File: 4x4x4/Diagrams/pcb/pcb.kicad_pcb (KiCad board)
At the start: 2 copper layers, 65.3 x 145.8 mm, 77 parts, among them J1 Conn_01x04_Female, J10 Conn_01x04_Female, J11 Conn_01x04_Female, J12 Conn_01x04_Female, J13 Conn_01x04_Female, J14 Conn_01x04_Female, J2 Conn_01x06_Female, J3 Conn_01x04_Female, J4 Conn_01x04_Female, J5 Conn_01x04_Female, J6 Conn_01x04_Female, J7 Conn_01x04_Female, J8 Conn_01x04_Female, J9 Conn_01x04_Female, Q1 2N2222, Q2 2N2222, Q3 2N2222, Q4 2N2222, U1 74HC595, U2 74HC595, U3 74HC595, U4 74HC595, U5 74HC595, U6 74HC595, U7 74HC595

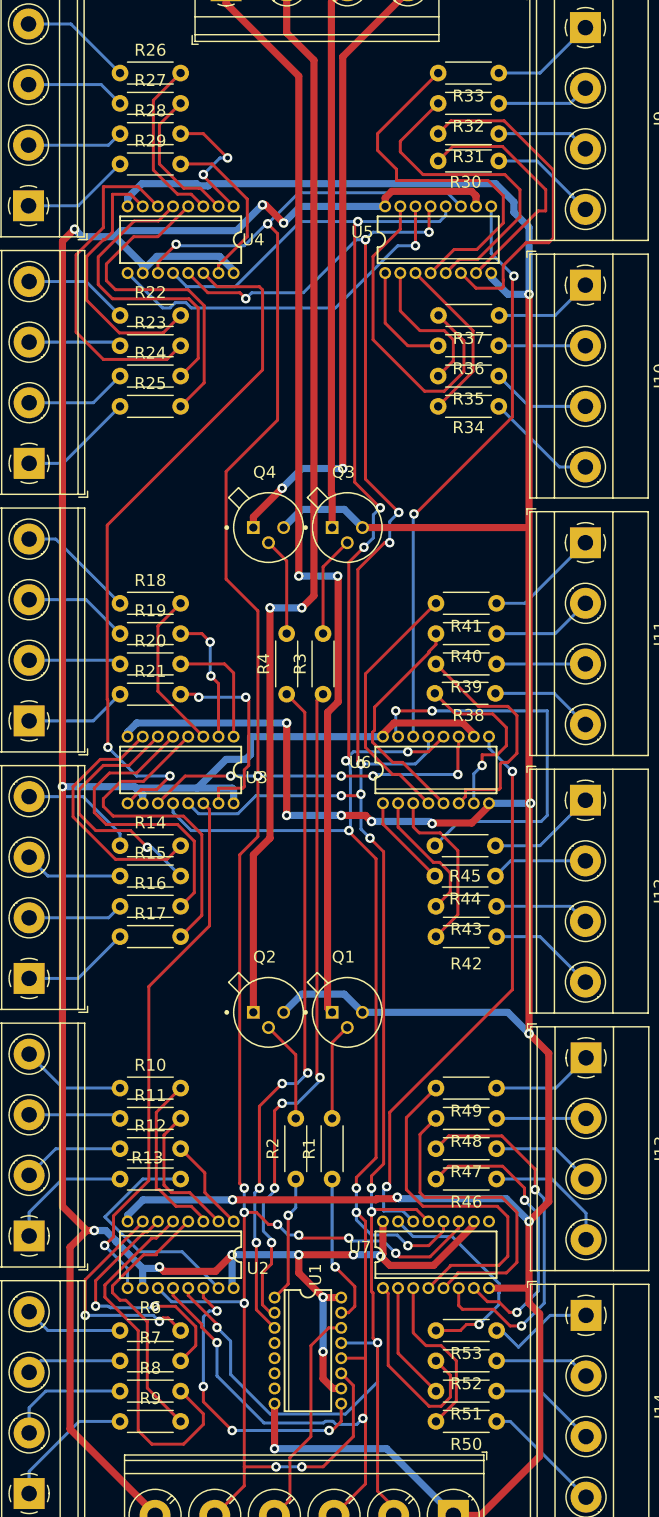
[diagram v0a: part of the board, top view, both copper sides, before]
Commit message: fixed wired connection pcb
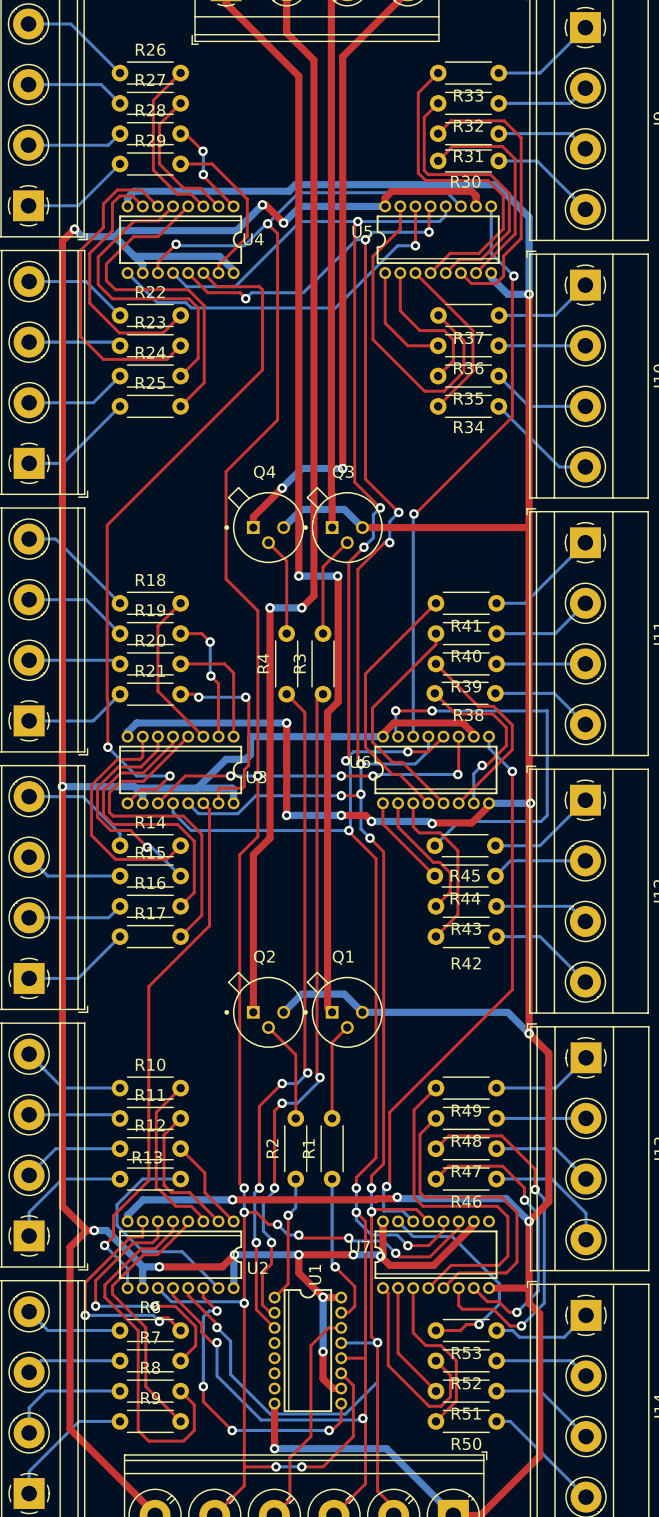
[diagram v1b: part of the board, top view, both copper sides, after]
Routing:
- net Net-(R31-Pad2): track 28.6 -> 24.4 mm
- net Net-(R33-Pad2): track 31.4 -> 27.4 mm
- net Net-(R32-Pad2): track 27.2 -> 24.0 mm
- net Net-(R39-Pad2): track 19.9 -> 16.9 mm
- net Net-(R28-Pad2): track 11.1 -> 8.18 mm
- net Net-(R30-Pad2): track 20.8 -> 18.3 mm
- net Net-(R15-Pad2): track 21.1 -> 19.0 mm
- net Net-(R23-Pad2): track 28.6 -> 27.2 mm
- net Net-(R16-Pad2): track 25.7 -> 24.5 mm
- net Net-(R14-Pad2): track 21.1 -> 19.9 mm
- net Net-(R13-Pad2): track 19.7 -> 18.7 mm
- net Net-(R22-Pad2): track 22.4 -> 21.6 mm
- net Net-(J14-Pad1): track 9.18 -> 8.49 mm
- net Net-(R7-Pad2): track 22.0 -> 22.7 mm
- net Net-(R6-Pad2): track 18.6 -> 19.2 mm
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
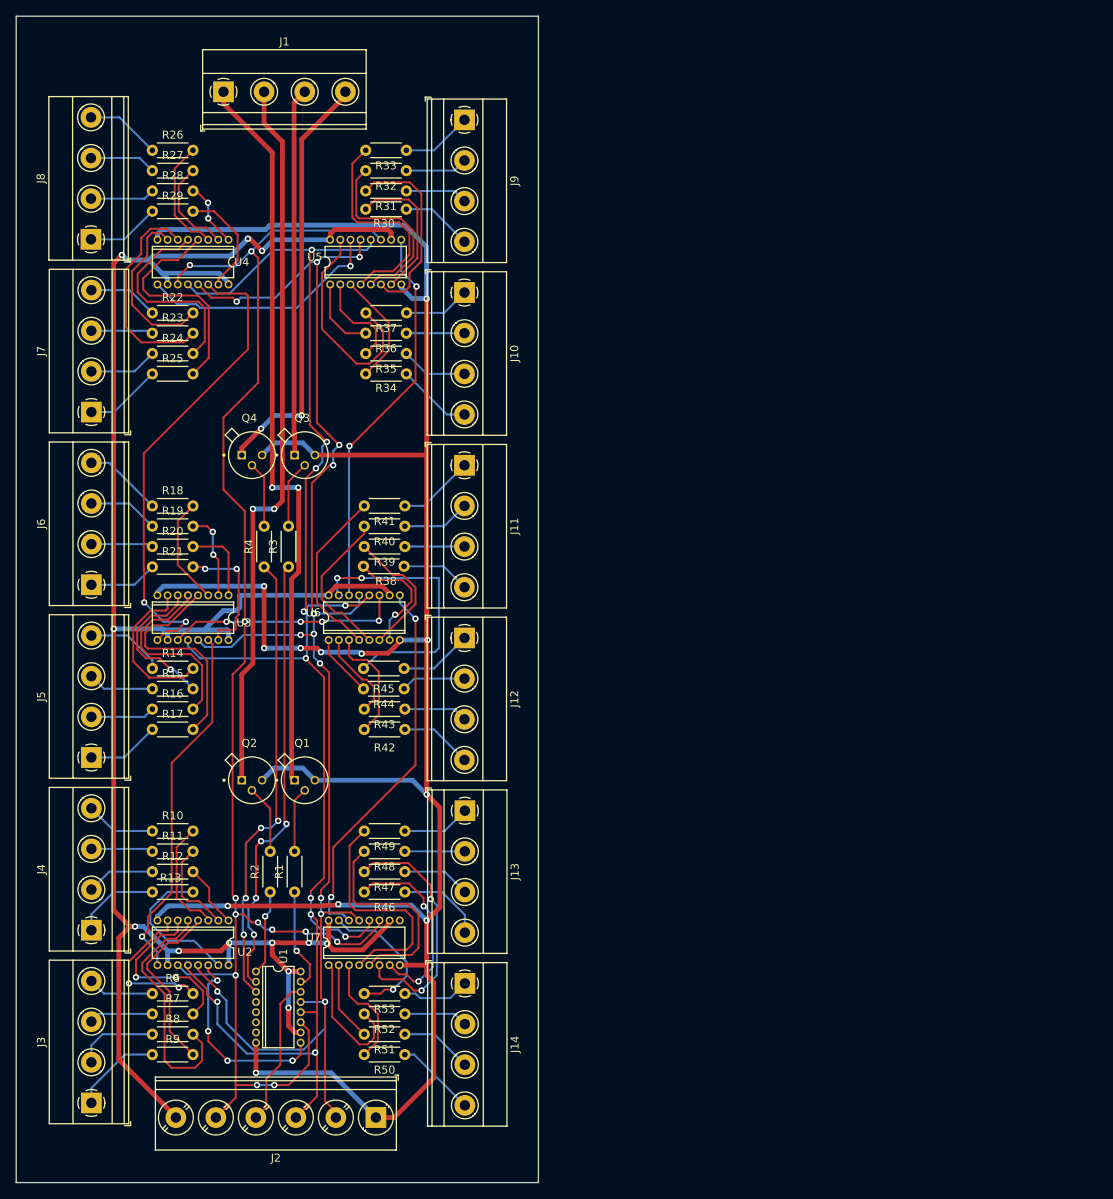
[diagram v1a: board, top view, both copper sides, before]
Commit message: redesign schematic
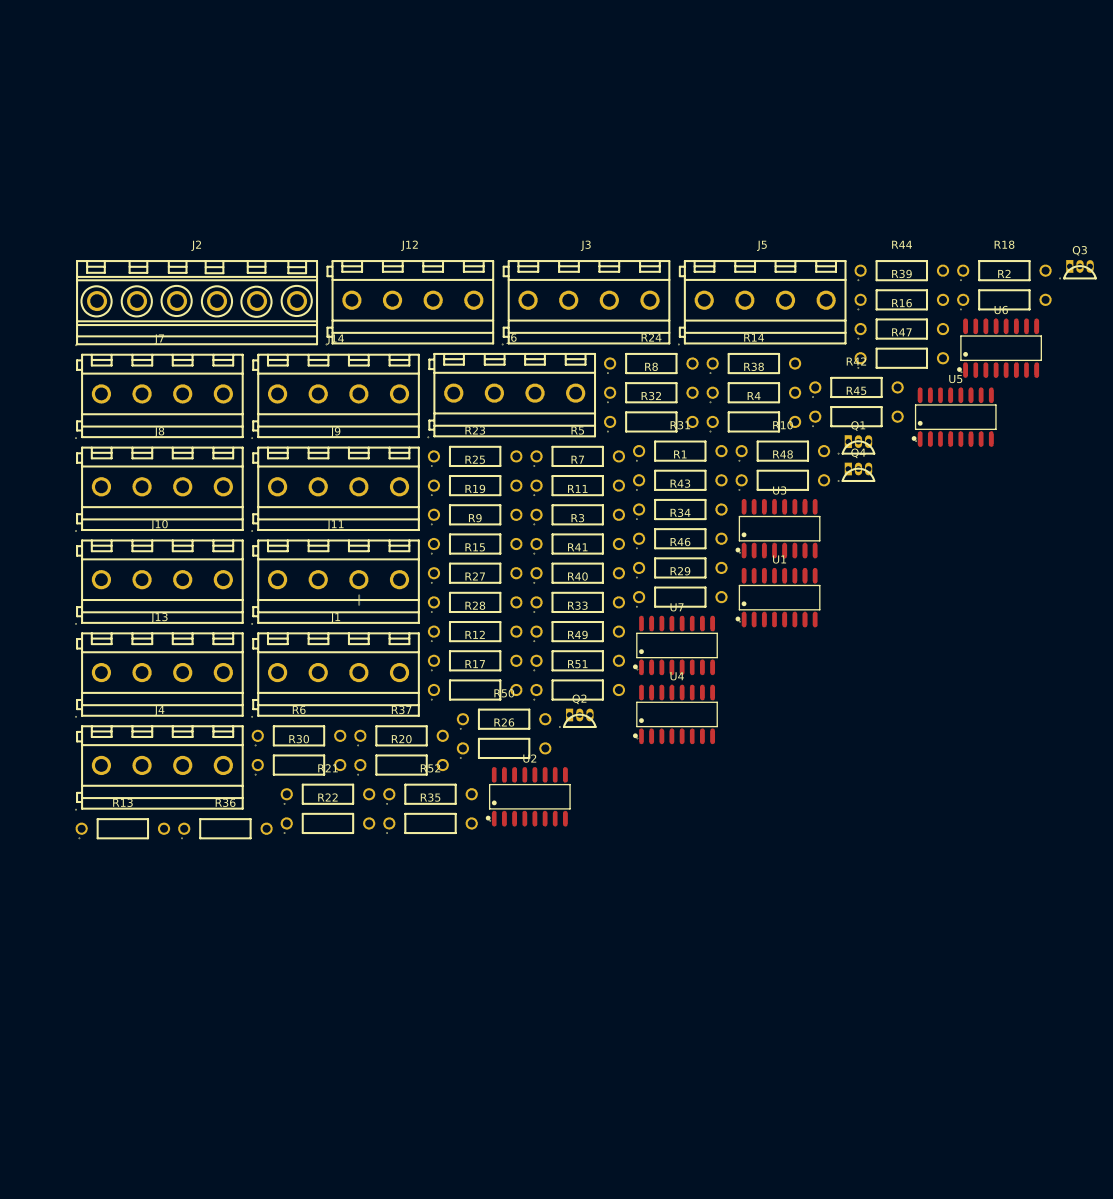
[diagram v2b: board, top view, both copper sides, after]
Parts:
- removed the J7 at (62.2, 68.3)
- removed the Q3 at (88.9, 73.7)
- removed the R33 at (101.6, 35.6)
- removed R53: 330, Resistor_THT:R_Axial_DIN0204_L3.6mm_D1.6mm_P5.08mm_Horizontal
- removed the R8 at (69.8, 146.1)
- removed the U7 at (96.3, 134.6)
- added Q1: 2N2222, 2N2222A:TO-92-3_L4.9-W3.7-P1.27-L, F.Cu at (158.1, 72.7)
- added R13: 330, 330R:RES-TH_BD2.4-L6.3-P10.30-D0.6, F.Cu at (66.2, 120.4)
- added R18: 330, 330R:RES-TH_BD2.4-L6.3-P10.30-D0.6, F.Cu at (176.4, 50.6)
- added R32: 330, 330R:RES-TH_BD2.4-L6.3-P10.30-D0.6, F.Cu at (132.2, 69.5)
- added R5: 330, 330R:RES-TH_BD2.4-L6.3-P10.30-D0.6, F.Cu at (123.0, 73.8)
- added U1: 74HC595D,118, 74HC595:SOIC-16_L9.9-W3.9-P1.27-LS6.0-BL, F.Cu at (148.3, 91.5)
- J1, J10, J11, J12, J13, J14, J3, J4, J5, J6, J8, J9: value Conn_01x04_Female -> DB128V-5_0-4P; footprint TerminalBlock_Phoenix:TerminalBlock_Phoenix_MKDS-1,5-4-5.08_1x04_P5.08mm_Horizontal -> DB128V-5.0-4P-GN-S:CONN-TH_DB128V-5.0-4P
- J2: value Conn_01x06_Female -> DB128V-5_0-6P; footprint TerminalBlock_Phoenix:TerminalBlock_Phoenix_PT-1,5-6-5.0-H_1x06_P5.00mm_Horizontal -> DB128V-5.0-6P-GN-S:CONN-TH_6P-P5.00_DB128V
- J7: renamed from Q1; value 2N2222 -> DB128V-5_0-4P; footprint 2N2222:TO127P584H533-3 -> DB128V-5.0-4P-GN-S:CONN-TH_DB128V-5.0-4P
- Q2, Q4: footprint 2N2222:TO127P584H533-3 -> 2N2222A:TO-92-3_L4.9-W3.7-P1.27-L
- Q3: renamed from R13; value 330 -> 2N2222; footprint Resistor_THT:R_Axial_DIN0204_L3.6mm_D1.6mm_P5.08mm_Horizontal -> 2N2222A:TO-92-3_L4.9-W3.7-P1.27-L
- R1, R2, R3, R4: footprint Resistor_THT:R_Axial_DIN0204_L3.6mm_D1.6mm_P5.08mm_Horizontal -> 1kR:RES-TH_BD2.4-L6.3-P10.30-D0.6
- R10, R11, R12, R14, R15, R16, R17, R19, R20, R21, R22, R23, R24, R25, R26, R27, R28, R29, R30, R31, R34, R35, R36, R37, R38, R39, R40, R41, R42, R43, R44, R45, R46, R47, R48, R49, R50, R51, R52, R6, R7, R9: footprint Resistor_THT:R_Axial_DIN0204_L3.6mm_D1.6mm_P5.08mm_Horizontal -> 330R:RES-TH_BD2.4-L6.3-P10.30-D0.6
- R33: renamed from R32; footprint Resistor_THT:R_Axial_DIN0204_L3.6mm_D1.6mm_P5.08mm_Horizontal -> 330R:RES-TH_BD2.4-L6.3-P10.30-D0.6
- R8: renamed from R18; footprint Resistor_THT:R_Axial_DIN0204_L3.6mm_D1.6mm_P5.08mm_Horizontal -> 330R:RES-TH_BD2.4-L6.3-P10.30-D0.6
- U2, U3, U4, U5, U6: value 74HC595 -> 74HC595D,118; footprint 74HC595:SO16 -> 74HC595:SOIC-16_L9.9-W3.9-P1.27-LS6.0-BL
- U7: renamed from U1; value 74HC595 -> 74HC595D,118; footprint 74HC595:SO16 -> 74HC595:SOIC-16_L9.9-W3.9-P1.27-LS6.0-BL
- moved Q3 139.4 mm to (185.8, 50.8)
- moved R2 117.9 mm to (176.4, 54.3), turned to 0 degrees
- moved J3 117.7 mm to (124.1, 54.6), turned to 0 degrees
- moved R16 105.0 mm to (163.5, 57.9)
- moved J2 104.3 mm to (75.4, 54.6), turned to 0 degrees
- moved J5 101.4 mm to (146.1, 54.6), turned to 0 degrees
- moved R10 92.0 mm to (148.7, 73.2)
- moved R47 89.3 mm to (163.5, 61.6), turned to 0 degrees
- moved R26 86.7 mm to (113.8, 110.3)
- moved U6 86.4 mm to (175.9, 60.3)
- moved R7 84.8 mm to (123.0, 77.5)
- moved R14 84.3 mm to (145.0, 62.2)
- moved U4 82.8 mm to (135.4, 106.1), turned to 0 degrees
- moved R29 81.7 mm to (135.8, 91.4)
- moved R44 81.3 mm to (163.5, 50.6), turned to 0 degrees
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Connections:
- J7 pad 1: Net-(J1-Pad1) -> Net-(J7-Pad1)
- J7 pad 2: Net-(Q1-Pad2) -> Net-(J7-Pad2)
- J7 pad 3: GND -> Net-(J7-Pad3)
- Q2 pad 1: Net-(J1-Pad2) -> Net-(J1-Pad3)
- Q3 pad 1: Net-(J4-Pad1) -> Net-(J1-Pad2)
- Q3 pad 2: Net-(R13-Pad2) -> Net-(Q3-Pad2)
- Q4 pad 1: Net-(J1-Pad4) -> Net-(J1-Pad1)
- R1 pad 2: Net-(Q1-Pad2) -> Net-(Q4-Pad2)
- R10 pad 1: Net-(J4-Pad4) -> Net-(J4-Pad3)
- R11 pad 1: Net-(J4-Pad3) -> Net-(J4-Pad2)
- R12 pad 1: Net-(J4-Pad2) -> Net-(J4-Pad1)
- R14 pad 1: Net-(J5-Pad4) -> Net-(J5-Pad3)
- R15 pad 1: Net-(J5-Pad3) -> Net-(J5-Pad2)
- R16 pad 1: Net-(J5-Pad2) -> Net-(J5-Pad1)
- R17 pad 1: Net-(J5-Pad1) -> Net-(J6-Pad4)
- R19 pad 1: Net-(J6-Pad3) -> Net-(J6-Pad2)
- R2 pad 2: Net-(Q2-Pad2) -> Net-(Q3-Pad2)
- R20 pad 1: Net-(J6-Pad2) -> Net-(J6-Pad1)
- R21 pad 1: Net-(J6-Pad1) -> Net-(J7-Pad4)
- R22 pad 1: Net-(J7-Pad4) -> Net-(J7-Pad3)
- R23 pad 1: Net-(J7-Pad3) -> Net-(J7-Pad2)
- R24 pad 1: Net-(J7-Pad2) -> Net-(J7-Pad1)
- R25 pad 1: Net-(J7-Pad1) -> Net-(J8-Pad4)
- R26 pad 1: Net-(J8-Pad4) -> Net-(J8-Pad3)
- R27 pad 1: Net-(J8-Pad3) -> Net-(J8-Pad2)
- R28 pad 1: Net-(J8-Pad2) -> Net-(J8-Pad1)
- R29 pad 1: Net-(J8-Pad1) -> Net-(J9-Pad4)
- R3 pad 2: Net-(Q3-Pad2) -> Net-(Q2-Pad2)
- R30 pad 1: Net-(J9-Pad4) -> Net-(J9-Pad3)
- R31 pad 1: Net-(J9-Pad3) -> Net-(J9-Pad2)
- R33 pad 1: Net-(J9-Pad2) -> Net-(J10-Pad4)
- R33 pad 2: Net-(R32-Pad2) (its old number) -> Net-(R33-Pad2)
- R34 pad 1: Net-(J10-Pad4) -> Net-(J10-Pad3)
- R35 pad 1: Net-(J10-Pad3) -> Net-(J10-Pad2)
- R36 pad 1: Net-(J10-Pad2) -> Net-(J10-Pad1)
- R37 pad 1: Net-(J10-Pad1) -> Net-(J11-Pad4)
- R38 pad 1: Net-(J11-Pad4) -> Net-(J11-Pad3)
- R39 pad 1: Net-(J11-Pad3) -> Net-(J11-Pad2)
- R4 pad 2: Net-(Q4-Pad2) -> Net-(Q1-Pad2)
- R40 pad 1: Net-(J11-Pad2) -> Net-(J11-Pad1)
- R41 pad 1: Net-(J11-Pad1) -> Net-(J12-Pad4)
- R42 pad 1: Net-(J12-Pad4) -> Net-(J12-Pad3)
- R43 pad 1: Net-(J12-Pad3) -> Net-(J12-Pad2)
- R44 pad 1: Net-(J12-Pad2) -> Net-(J12-Pad1)
- R45 pad 1: Net-(J12-Pad1) -> Net-(J13-Pad4)
- R46 pad 1: Net-(J13-Pad4) -> Net-(J13-Pad3)
- R47 pad 1: Net-(J13-Pad3) -> Net-(J13-Pad2)
- R48 pad 1: Net-(J13-Pad2) -> Net-(J13-Pad1)
- R49 pad 1: Net-(J13-Pad1) -> Net-(J14-Pad4)
- R50 pad 1: Net-(J14-Pad4) -> Net-(J14-Pad3)
- R51 pad 1: Net-(J14-Pad3) -> Net-(J14-Pad2)
- R52 pad 1: Net-(J14-Pad2) -> Net-(J14-Pad1)
- R6 pad 1: Net-(J3-Pad4) -> Net-(J3-Pad3)
- R7 pad 1: Net-(J3-Pad3) -> Net-(J3-Pad2)
- R8 pad 1: Net-(J6-Pad4) -> Net-(J3-Pad1)
- R8 pad 2: Net-(R18-Pad2) -> Net-(R8-Pad2)
- R9 pad 1: Net-(J3-Pad1) -> Net-(J4-Pad4)
- U2 pad 1: Net-(R12-Pad2) -> Net-(R11-Pad2)
- U2 pad 11: Net-(J2-Pad5) -> Net-(J2-Pad2)
- U2 pad 13: Net-(J2-Pad2) -> Net-(J2-Pad4)
- U2 pad 15: Net-(R13-Pad2) -> Net-(R12-Pad2)
- U2 pad 2: Net-(R11-Pad2) -> Net-(R10-Pad2)
- U2 pad 3: Net-(R10-Pad2) -> Net-(R9-Pad2)
- U2 pad 4: Net-(R9-Pad2) -> Net-(R8-Pad2)
- U2 pad 5: Net-(R8-Pad2) -> Net-(R7-Pad2)
- U2 pad 6: Net-(R7-Pad2) -> Net-(R6-Pad2)
- U2 pad 7: Net-(R6-Pad2) -> Net-(R5-Pad2)
- U3 pad 1: Net-(R20-Pad2) -> Net-(R19-Pad2)
- U3 pad 11: Net-(J2-Pad5) -> Net-(J2-Pad2)
- U3 pad 13: Net-(J2-Pad2) -> Net-(J2-Pad4)
- U3 pad 15: Net-(R21-Pad2) -> Net-(R20-Pad2)
- U3 pad 2: Net-(R19-Pad2) -> Net-(R18-Pad2)
- U3 pad 3: Net-(R18-Pad2) -> Net-(R17-Pad2)
- U3 pad 4: Net-(R17-Pad2) -> Net-(R16-Pad2)
- U3 pad 5: Net-(R16-Pad2) -> Net-(R15-Pad2)
- U3 pad 6: Net-(R15-Pad2) -> Net-(R14-Pad2)
- U3 pad 7: Net-(R14-Pad2) -> Net-(R13-Pad2)
- U4 pad 1: Net-(R28-Pad2) -> Net-(R27-Pad2)
- U4 pad 11: Net-(J2-Pad5) -> Net-(J2-Pad2)
- U4 pad 13: Net-(J2-Pad2) -> Net-(J2-Pad4)
- U4 pad 15: Net-(R29-Pad2) -> Net-(R28-Pad2)
- U4 pad 2: Net-(R27-Pad2) -> Net-(R26-Pad2)
- U4 pad 3: Net-(R26-Pad2) -> Net-(R25-Pad2)
- U4 pad 4: Net-(R25-Pad2) -> Net-(R24-Pad2)
- U4 pad 5: Net-(R24-Pad2) -> Net-(R23-Pad2)
- U4 pad 6: Net-(R23-Pad2) -> Net-(R22-Pad2)
- U4 pad 7: Net-(R22-Pad2) -> Net-(R21-Pad2)
- U5 pad 1: Net-(R36-Pad2) -> Net-(R35-Pad2)
- U5 pad 11: Net-(J2-Pad5) -> Net-(J2-Pad2)
- U5 pad 13: Net-(J2-Pad2) -> Net-(J2-Pad4)
- U5 pad 15: Net-(R37-Pad2) -> Net-(R36-Pad2)
- U5 pad 2: Net-(R35-Pad2) -> Net-(R34-Pad2)
- U5 pad 3: Net-(R34-Pad2) -> Net-(R33-Pad2)
- U5 pad 5: Net-(R32-Pad2) (its old number) -> Net-(R31-Pad2)
- U5 pad 6: Net-(R31-Pad2) -> Net-(R30-Pad2)
- U5 pad 7: Net-(R30-Pad2) -> Net-(R29-Pad2)
- U6 pad 1: Net-(R44-Pad2) -> Net-(R43-Pad2)
- U6 pad 11: Net-(J2-Pad5) -> Net-(J2-Pad2)
- U6 pad 13: Net-(J2-Pad2) -> Net-(J2-Pad4)
- U6 pad 15: Net-(R45-Pad2) -> Net-(R44-Pad2)
- U6 pad 2: Net-(R43-Pad2) -> Net-(R42-Pad2)
- U6 pad 3: Net-(R42-Pad2) -> Net-(R41-Pad2)
- U6 pad 4: Net-(R41-Pad2) -> Net-(R40-Pad2)
- U6 pad 5: Net-(R40-Pad2) -> Net-(R39-Pad2)
- U6 pad 6: Net-(R39-Pad2) -> Net-(R38-Pad2)
- U6 pad 7: Net-(R38-Pad2) -> Net-(R37-Pad2)
- U7 pad 1: Net-(R2-Pad1) -> Net-(R51-Pad2)
- U7 pad 11: Net-(J2-Pad5) -> Net-(J2-Pad2)
- U7 pad 13: Net-(J2-Pad2) -> Net-(J2-Pad4)
- U7 pad 14: Net-(J2-Pad4) -> Net-(U6-Pad9)
- U7 pad 15: Net-(R1-Pad1) -> Net-(R52-Pad2)
- U7 pad 2: Net-(R3-Pad1) -> Net-(R50-Pad2)
- U7 pad 3: Net-(R4-Pad1) -> Net-(R49-Pad2)
- U7 pad 4: unconnected-(U1-Pad4) -> Net-(R48-Pad2)
- U7 pad 5: unconnected-(U1-Pad5) -> Net-(R47-Pad2)
- U7 pad 6: unconnected-(U1-Pad6) -> Net-(R46-Pad2)
- U7 pad 7: unconnected-(U1-Pad7) -> Net-(R45-Pad2)
- U7 pad 9: Net-(U1-Pad9) -> unconnected-(U7-Pad9)
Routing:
- net GND: track 302.5 -> 0.00 mm, vias 12 -> 0
- net Net-(J2-Pad6): track 266.3 -> 0.00 mm, vias 12 -> 0
- net Net-(J2-Pad5): track 216.7 -> 0.00 mm, vias 16 -> 0
- net Net-(J2-Pad3): track 201.0 -> 0.00 mm, vias 11 -> 0
- net Net-(J2-Pad2): track 195.4 -> 1.20 mm, vias 13 -> 0
- net Net-(J1-Pad1): track 92.4 -> 0.00 mm, vias 2 -> 0
- net Net-(J1-Pad2): track 90.7 -> 0.00 mm, vias 2 -> 0
- net Net-(U3-Pad9): track 60.0 -> 0.00 mm, vias 2 -> 0
- net Net-(R4-Pad1): track 57.1 -> 0.00 mm, vias 4 -> 0
- net Net-(R3-Pad1): track 56.1 -> 0.00 mm, vias 4 -> 0
- net Net-(J1-Pad4): track 52.8 -> 0.00 mm, vias 2 -> 0
- net Net-(U5-Pad9): track 48.8 -> 0.00 mm, vias 2 -> 0
- net Net-(U6-Pad9): track 47.9 -> 0.00 mm, vias 2 -> 0
- net Net-(J1-Pad3): track 46.0 -> 0.00 mm
- net Net-(U2-Pad9): track 45.3 -> 0.00 mm, vias 1 -> 0
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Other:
- board outline removed
